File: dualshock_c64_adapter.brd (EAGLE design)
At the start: 57 x 43 mm, 9 parts, among them J2 PS2_DUALSHOCK, M1 ARDUINO-PRO-MINI-3.3V

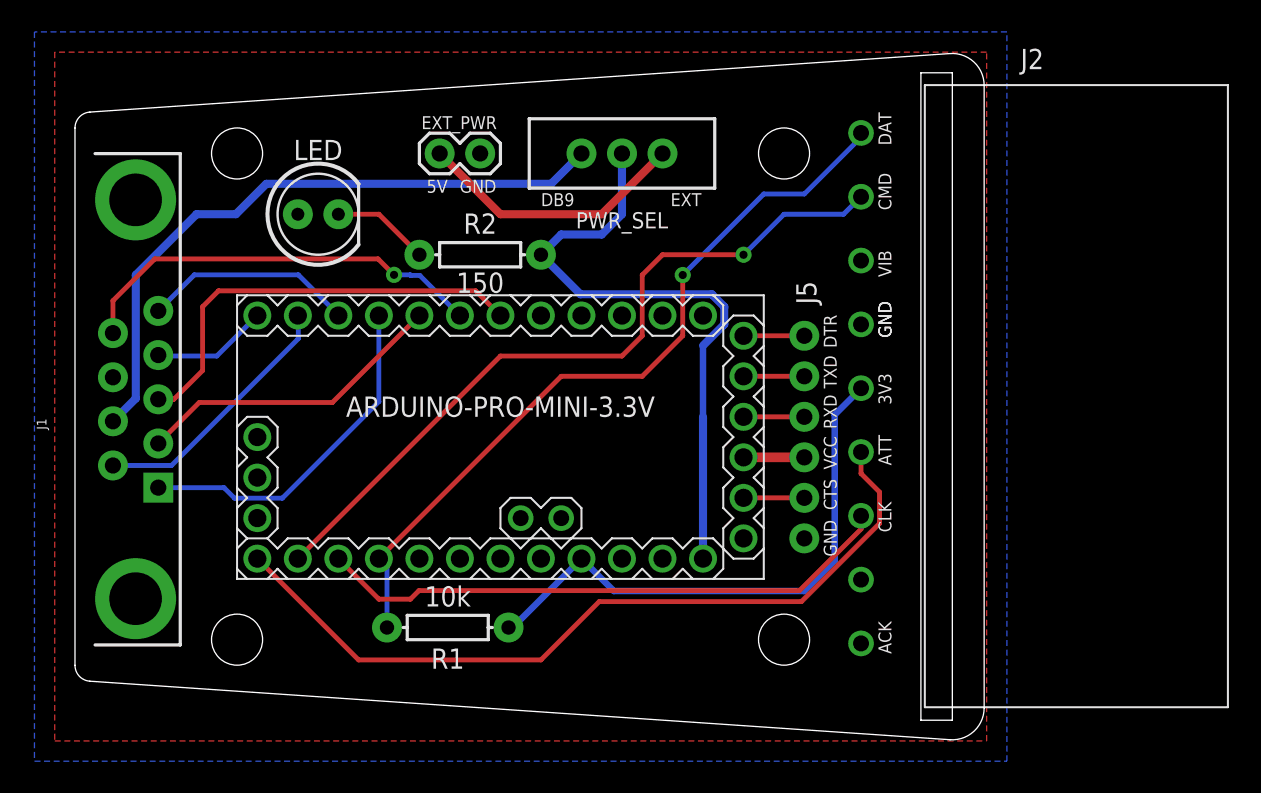
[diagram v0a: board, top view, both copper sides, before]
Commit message: Some minor changes on PCB design
Rerouting and dimension change on pins
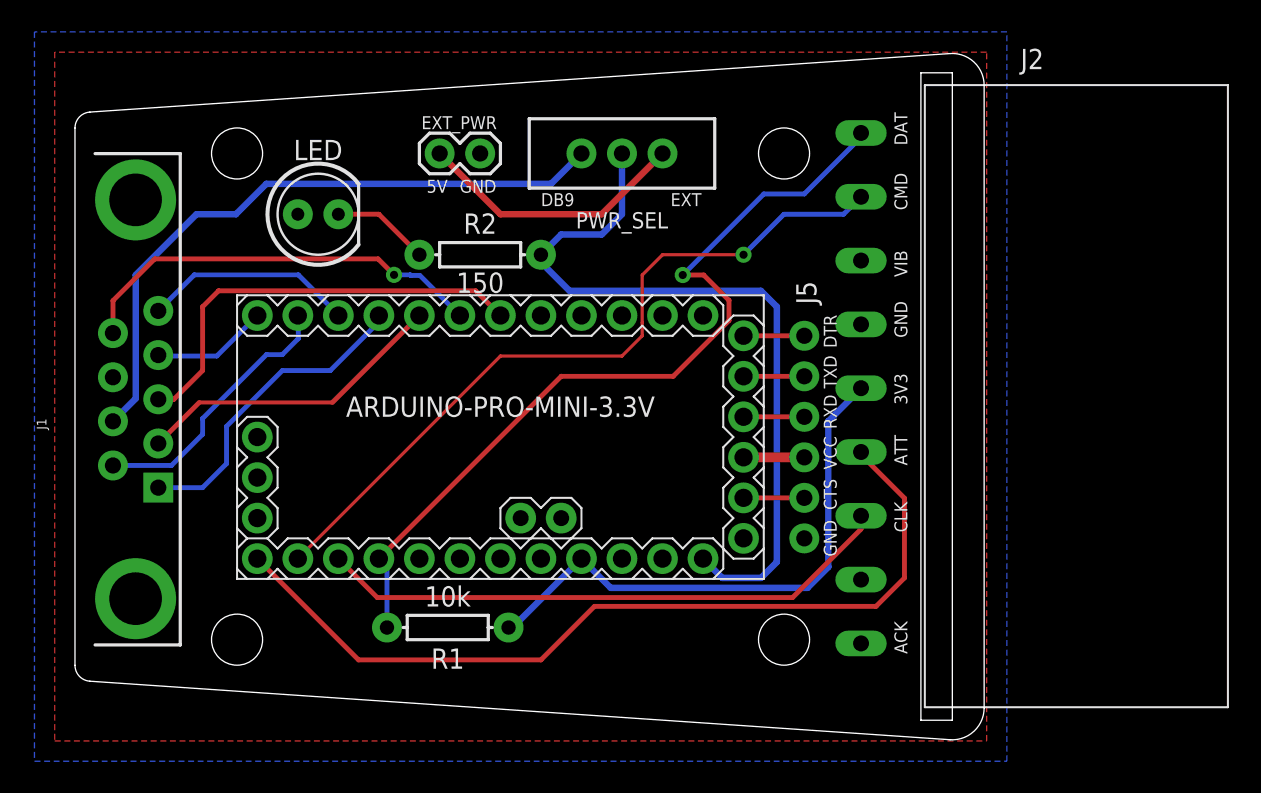
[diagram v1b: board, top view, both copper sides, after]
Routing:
- net 5V: track 39.1 -> 47.9 mm
- net D13: track 48.2 -> 52.5 mm
- net D10: track 50.1 -> 54.4 mm
- net UP: track 22.0 -> 19.9 mm
- net FIRE: track 16.4 -> 17.0 mm
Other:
- board text added: "V2.13"
